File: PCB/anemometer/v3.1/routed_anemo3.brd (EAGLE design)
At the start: 100 x 80 mm, 66 parts, among them IC1 AD8223, IC2 AD8223, IC3 AD8223, IC4 AD8223, IC6 TL072D, J1 RJ12STRAIGHT-I2C, J2 RJ12STRAIGHT-I2C, T1 BC846, T2 BC846, T3 BC846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

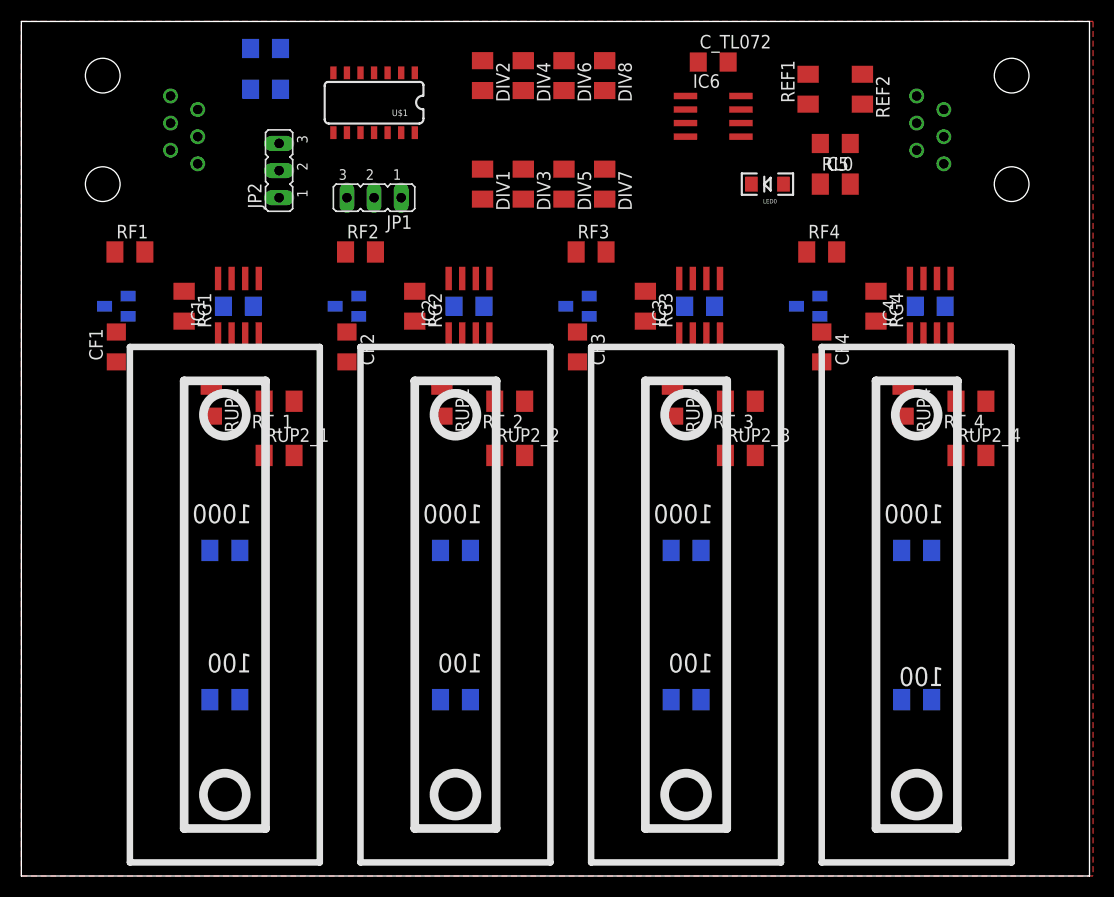
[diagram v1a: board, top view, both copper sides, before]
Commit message: Autorouting completed, ground plane added on both sides
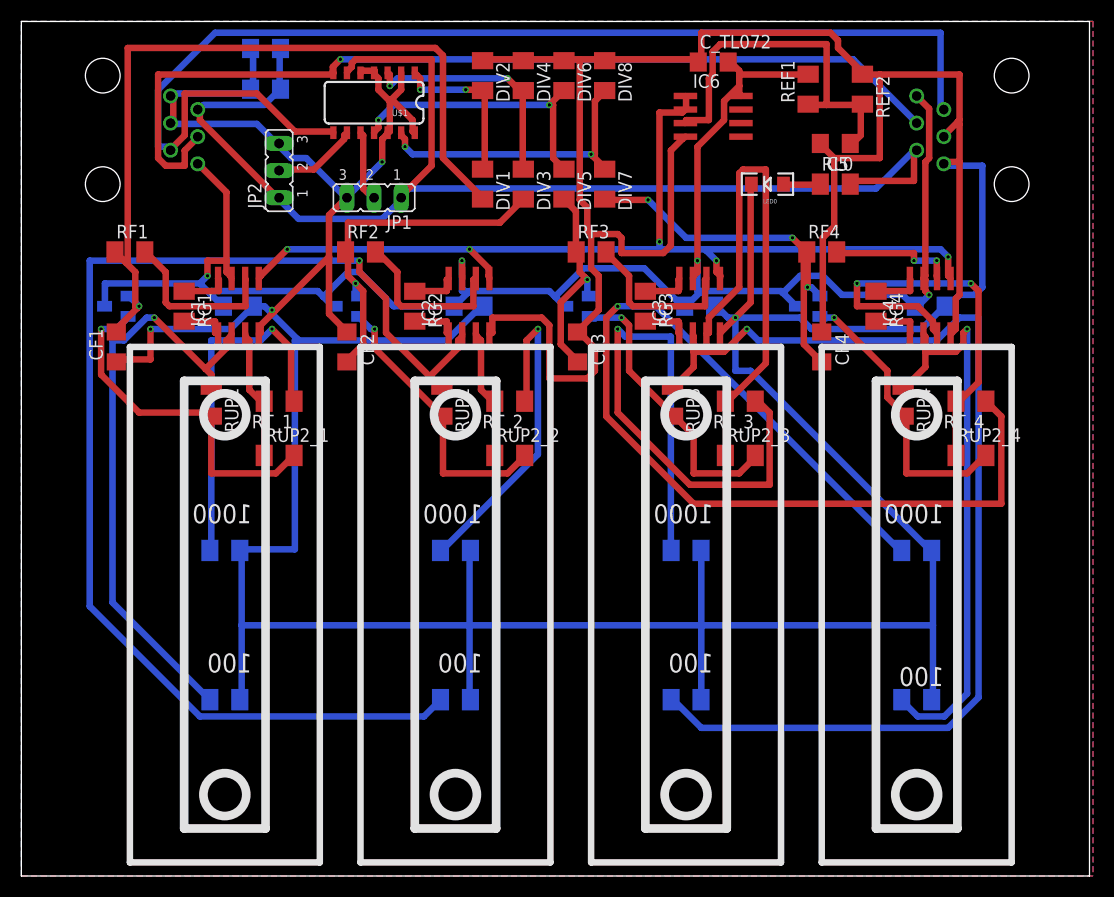
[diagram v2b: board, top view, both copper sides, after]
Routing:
- net GND: track 0.00 -> 533.5 mm, vias 0 -> 4
- net VCC: track 0.00 -> 169.1 mm, vias 0 -> 4
- net 5V: track 0.00 -> 119.3 mm
- net IN-2: track 0.00 -> 115.7 mm, vias 0 -> 1
- net SCL: track 0.00 -> 110.9 mm
- net IN-3: track 0.00 -> 101.3 mm, vias 0 -> 1
- net N$29: track 0.00 -> 97.4 mm, vias 0 -> 1
- net REF: track 0.00 -> 91.5 mm, vias 0 -> 5
- net SDA: track 0.00 -> 88.3 mm, vias 0 -> 1
- net OUT1: track 0.00 -> 75.8 mm, vias 0 -> 1
- net N$27: track 0.00 -> 58.7 mm, vias 0 -> 1
- net IN-1: track 0.00 -> 55.1 mm, vias 0 -> 1
- net IN-4: track 0.00 -> 53.2 mm, vias 0 -> 1
- net IN+3: track 0.00 -> 47.6 mm
- net IN+4: track 0.00 -> 39.3 mm, vias 0 -> 2
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- added copper zone on layer 16, net GND
